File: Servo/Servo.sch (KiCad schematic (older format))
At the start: 19 parts, among them J1 Pi, J10 Motor2, J11 Conn_01x03, J12 Conn_01x03, J13 Conn_01x03, J14 Conn_01x03, J2 ISP, J3 Power, J4 Conn_01x03, J5 Conn_01x03, J6 Servo 1, J7 Servo 2, J8 Motor1, J9 Laser, U1 ATtiny2313A-PU, U2 L293D

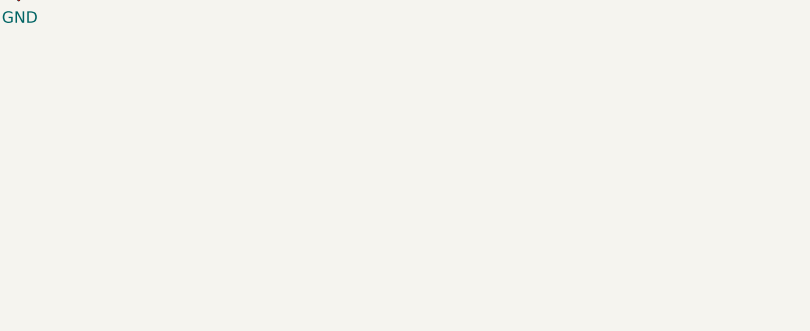
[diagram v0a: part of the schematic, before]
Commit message: Created Data sheet & Updated schematic
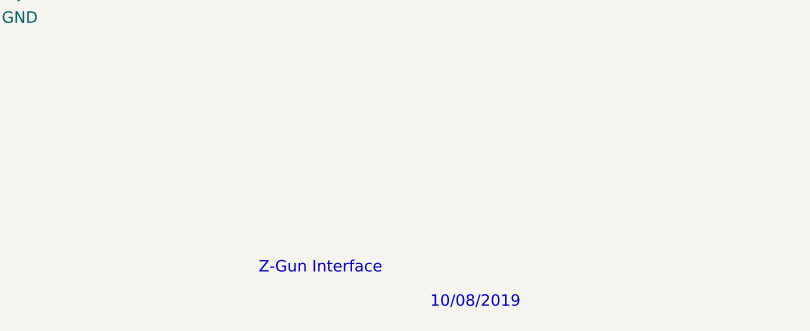
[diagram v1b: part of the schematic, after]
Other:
- note added: "10/08/2019"
- note added: "Z-Gun Interface"
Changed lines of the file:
@@
 EESchema Schematic File Version 4
 LIBS:Servo-cache
-EELAYER 29 0
+EELAYER 30 0
 EELAYER END
 $Descr A4 11693 8268
@@
 	1    0    0    -1
 $EndComp
+Text Notes 7600 7500 0    50   ~ 0
+Z-Gun Interface
+Text Notes 8350 7650 0    50   ~ 0
+10/08/2019
 $EndSCHEMATC
